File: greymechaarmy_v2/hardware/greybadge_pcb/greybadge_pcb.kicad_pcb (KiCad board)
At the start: 2 copper layers, 75 x 99 mm, 154 parts, among them J1 Conn_02x05_Row_Letter_First, J2 Conn_02x05_Row_Letter_First, J3 Conn_02x05_Row_Letter_First, J4 JST PH S2B, J5 USB_C_Receptacle_USB2.0, Q1 2N7002, Q2 Q_NMOS_GSD, SW1 SW_Push, SW10 SW_Push, SW2 SW_Push, SW3 SW_Push, SW4 SW_Push, SW5 SW_Push, SW6 SW_Push, SW7 SW_Push, SW8 SW_SPDT, SW9 SW_Push, U1 APS6404L-3SQR-SN_C5333729, U10 AMS1117-3.3, U2 TLV73311PDBV, U3 TLV73325PDBV, U4 GC9A01_IPS_display, U5 BQ24075, U6 W25Q128JVS, U7 RP2350_60QFN, U8 ECP5U_25_CABGA256, U9 W25Q128JVSIM, X1 SiT2001B, Y1 12Mhz

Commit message: feat: update jlcpcb header component + label
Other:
- board text added: "GreyMecha/Army_v2"
- board text removed: "GreyMecha/Army"

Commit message: refactor: move jtag and fpga flash
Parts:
- moved JP5 38.6 mm to (124.8, 81.3), turned to -90 degrees
- moved R46 35.8 mm to (125.1, 78.5), turned to 0 degrees
- moved JP4 34.2 mm to (122.2, 81.4), turned to -90 degrees
- moved JP3 30.0 mm to (119.6, 81.3), turned to -90 degrees
- moved R38 29.4 mm to (120.9, 78.5), turned to 180 degrees
- moved JP2 26.2 mm to (117.0, 81.3), turned to -90 degrees
- moved JP1 22.9 mm to (114.4, 81.3), turned to -90 degrees
- moved TP4 7.81 mm to (118.0, 94.5)
- moved TP5 6.64 mm to (118.0, 92.0)
- moved R8 2.00 mm to (93.9, 91.0), turned to 0 degrees
- moved R45 1.74 mm to (103.0, 72.6)
- moved R44 1.27 mm to (90.1, 79.8)
- moved U9 1.27 mm to (96.5, 75.5)
- moved R42 1.27 mm to (90.1, 78.2)
- moved R39 1.27 mm to (90.1, 81.4)
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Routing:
- net GPIO20: track 71.4 -> 19.1 mm
- net GPIO19: track 68.4 -> 21.0 mm
- net GPIO18: track 66.4 -> 24.4 mm
- net GPIO17: track 63.8 -> 27.5 mm
- net GPIO16: track 62.0 -> 31.1 mm
- net fpga_tdo: track 27.1 -> 13.9 mm
- net fpga_tms: track 23.4 -> 12.5 mm
- net fpga_tdi: track 27.2 -> 17.3 mm
- net +3V3: track 356.5 -> 346.6 mm
- net fpga_tck: track 29.4 -> 20.1 mm
- net creset: track 33.4 -> 25.2 mm
- net C15: track 37.7 -> 32.7 mm
- net B4: track 46.6 -> 51.6 mm
- net A15: track 38.4 -> 33.6 mm
- net B15: track 37.2 -> 33.2 mm
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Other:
- board text added: "crst/GP20 tck/GP19 tdi/GP18 tms/GP17 tdo/GP16"
- board text added: "github.com/NUSGreyhats pcb: hackin7, itsme-zeix, sayo art: shuqing"
- board text removed: "GP20/crst GP19/tck GP18/tdi GP17/tms GP16/tdo"
- board text removed: "github.com/NUSGreyhats pcb: hackin7 & itsme-zeix art: shuqing"

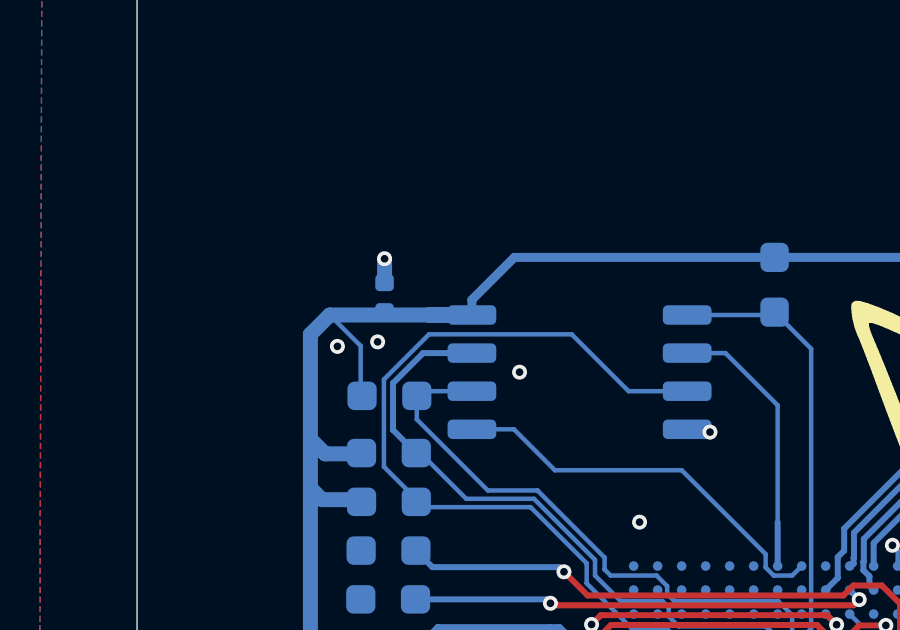
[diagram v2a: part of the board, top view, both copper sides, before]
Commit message: fix: resolve 1 DRC warning
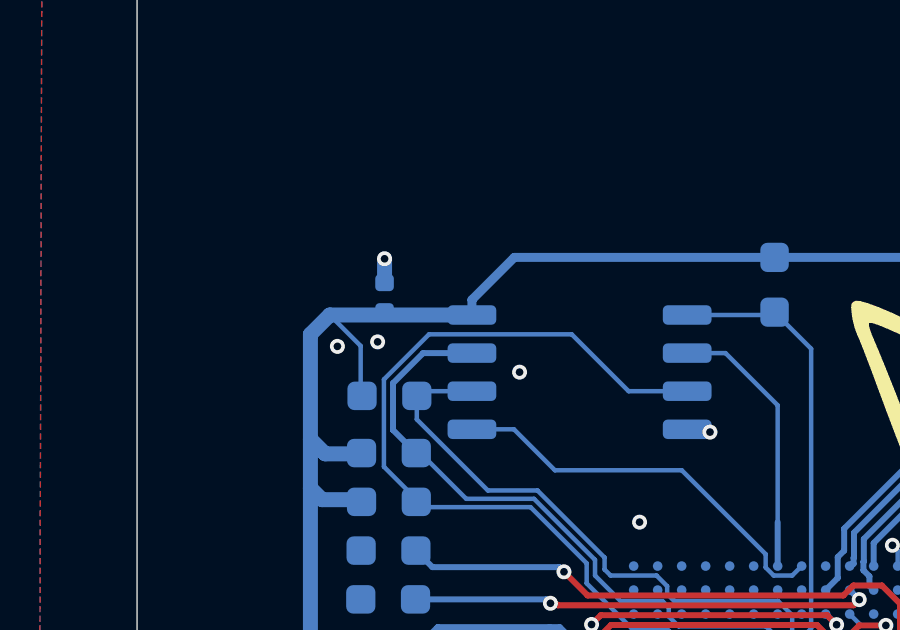
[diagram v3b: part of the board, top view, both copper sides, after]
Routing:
- net +3V3: track 346.6 -> 345.1 mm
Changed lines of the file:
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@@
-	)
-	(segment
-		(start 92.9125 73.595)
-		(end 91.450159 73.595)
-		(width 0.5)
-		(layer "B.Cu")
-		(net 2)
 	)
 	(segment

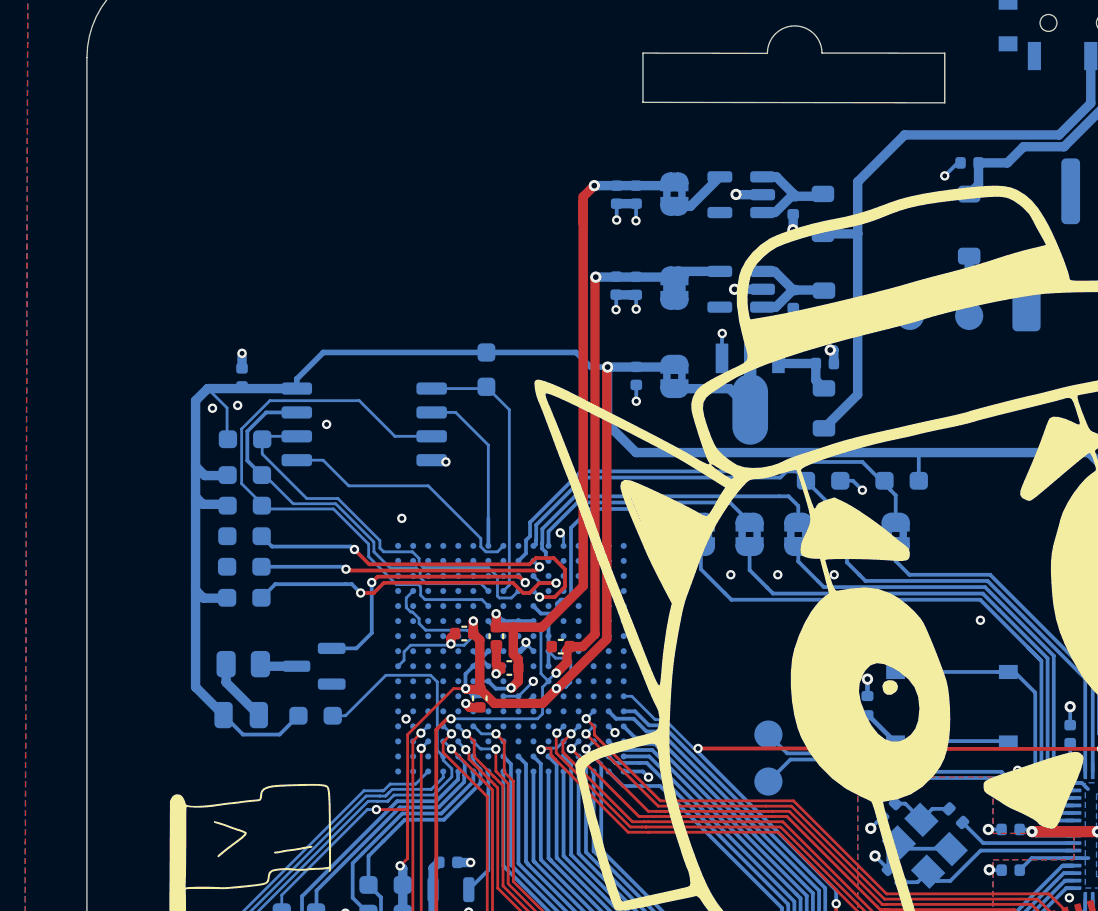
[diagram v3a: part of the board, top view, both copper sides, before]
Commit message: feat: add additional pmod header with differential lines
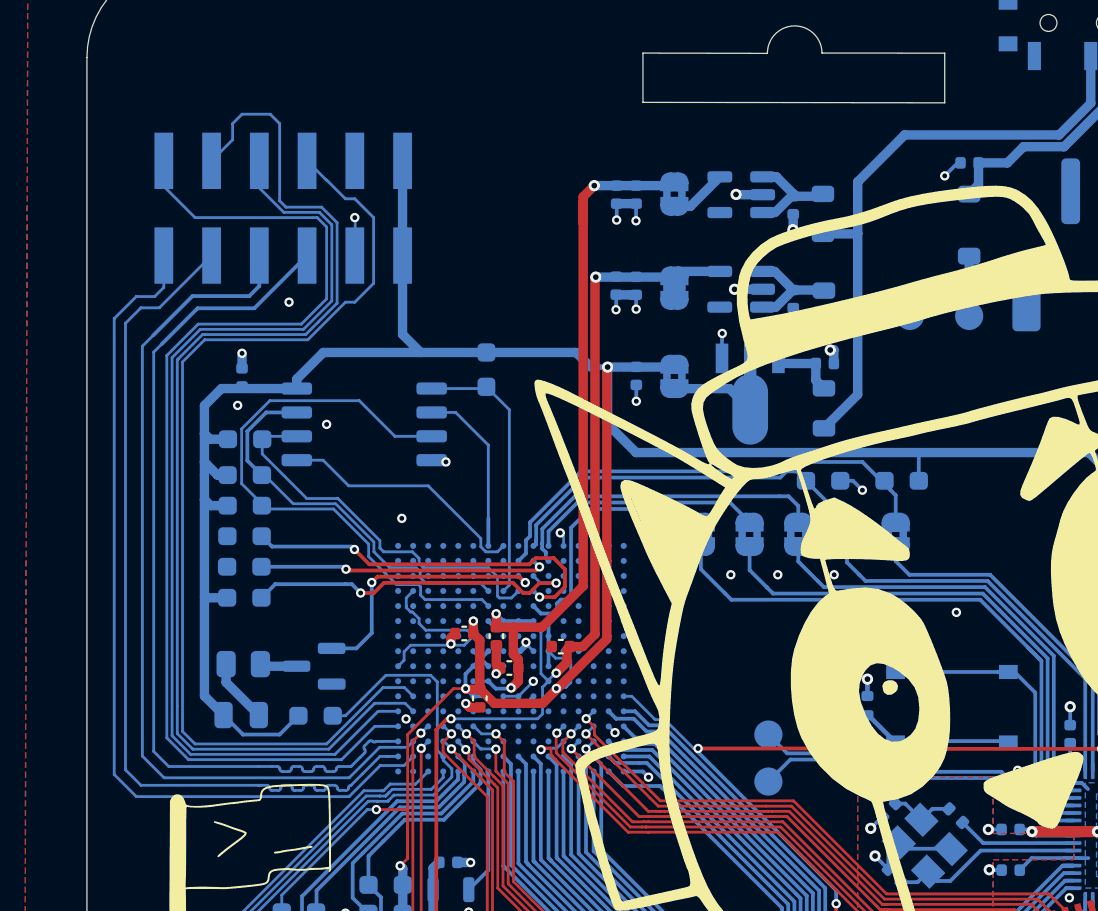
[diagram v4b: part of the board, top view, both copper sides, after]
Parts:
- added J6: Conn_02x05_Row_Letter_First, Connector_PinSocket_2.54mm:PinSocket_2x06_P2.54mm_Vertical_SMD, B.Cu at (92.2, 64.0)
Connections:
- U8 pad B1: unconnected-(U8G-PL2A/+/HS/LDQ8-PadB1) -> PMOD1+
- U8 pad B2: unconnected-(U8G-PL2B/-/HS/LDQ8-PadB2) -> PMOD1-
- U8 pad C1: unconnected-(U8G-PL5A/+/HS/LDQ8-PadC1) -> PMOD2+
- U8 pad C2: unconnected-(U8G-PL5B/-/HS/LDQ8-PadC2) -> PMOD2-
- U8 pad D1: unconnected-(U8G-PL8A/+/HS/LDQS8-PadD1) -> D1
- U8 pad E1: unconnected-(U8G-PL11D/-/LDQ8-PadE1) -> E1
- U8 pad E2: unconnected-(U8G-PL8B/-/HS/LDQSN8-PadE2) -> E2
- U8 pad F2: unconnected-(U8G-PL11C/+/LDQ8-PadF2) -> F2
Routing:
- net E2: track 0.00 -> 61.0 mm
- net D1: track 0.00 -> 58.3 mm
- net F2: track 0.00 -> 53.8 mm
- net E1: track 0.00 -> 53.4 mm
- net PMOD2-: track 0.00 -> 47.7 mm
- net PMOD2+: track 0.00 -> 47.6 mm
- net PMOD1-: track 0.00 -> 46.5 mm
- net PMOD1+: track 0.00 -> 46.5 mm
- net +3V3: track 345.1 -> 351.8 mm
- net GND: track 112.7 -> 114.8 mm, vias 88 -> 89
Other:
- board text added: "3.3V, GND, F2, E1, E2, D1 3.3V, GND, C1, C2, B1, B2"
